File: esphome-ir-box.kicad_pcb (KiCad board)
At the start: 2 copper layers, 32 x 55.8 mm, 16 parts, among them J1 Conn_01x15_Female, J2 Conn_01x15_Female, J3 Conn_01x15_Male, J4 Conn_01x15_Male, Q1 2N7000, Q2 2N7000, Q3 2N7000, U1 VS1838B

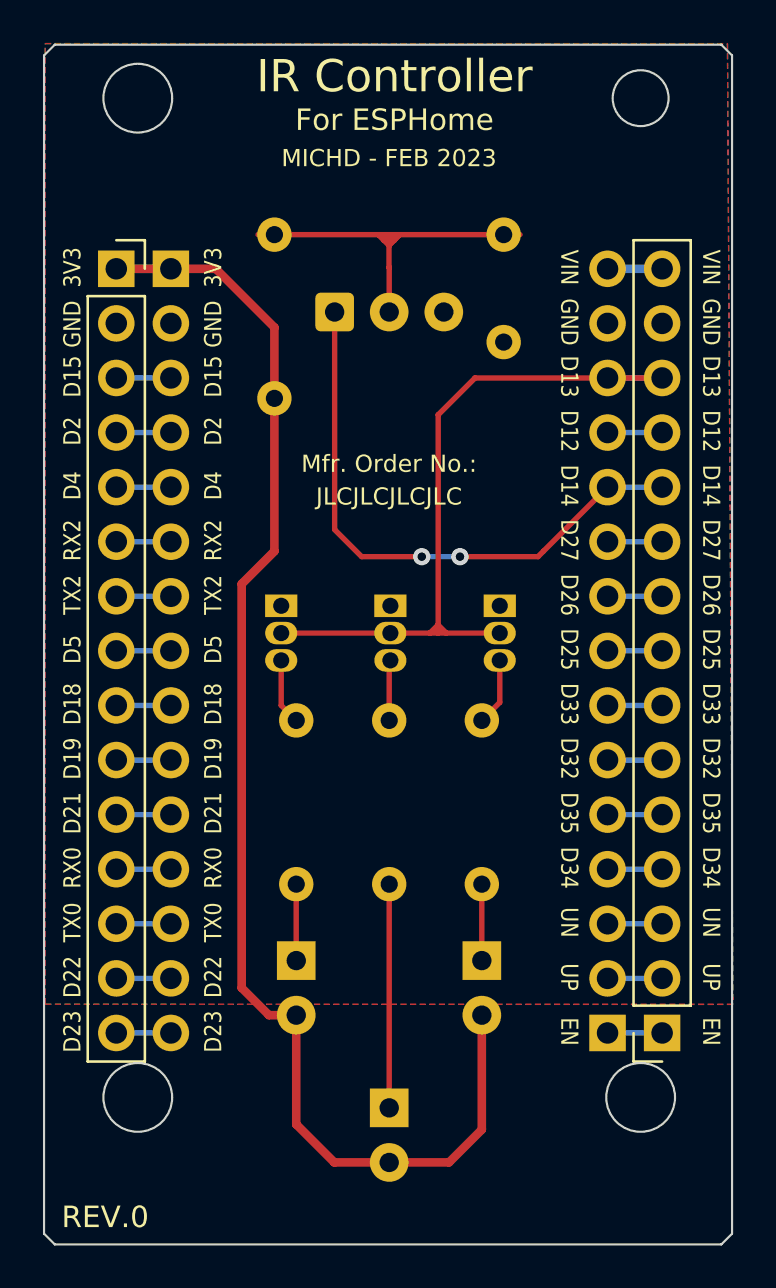
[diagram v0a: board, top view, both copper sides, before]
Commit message: Fix VS1813B pinout, KiCad 7 tweaks
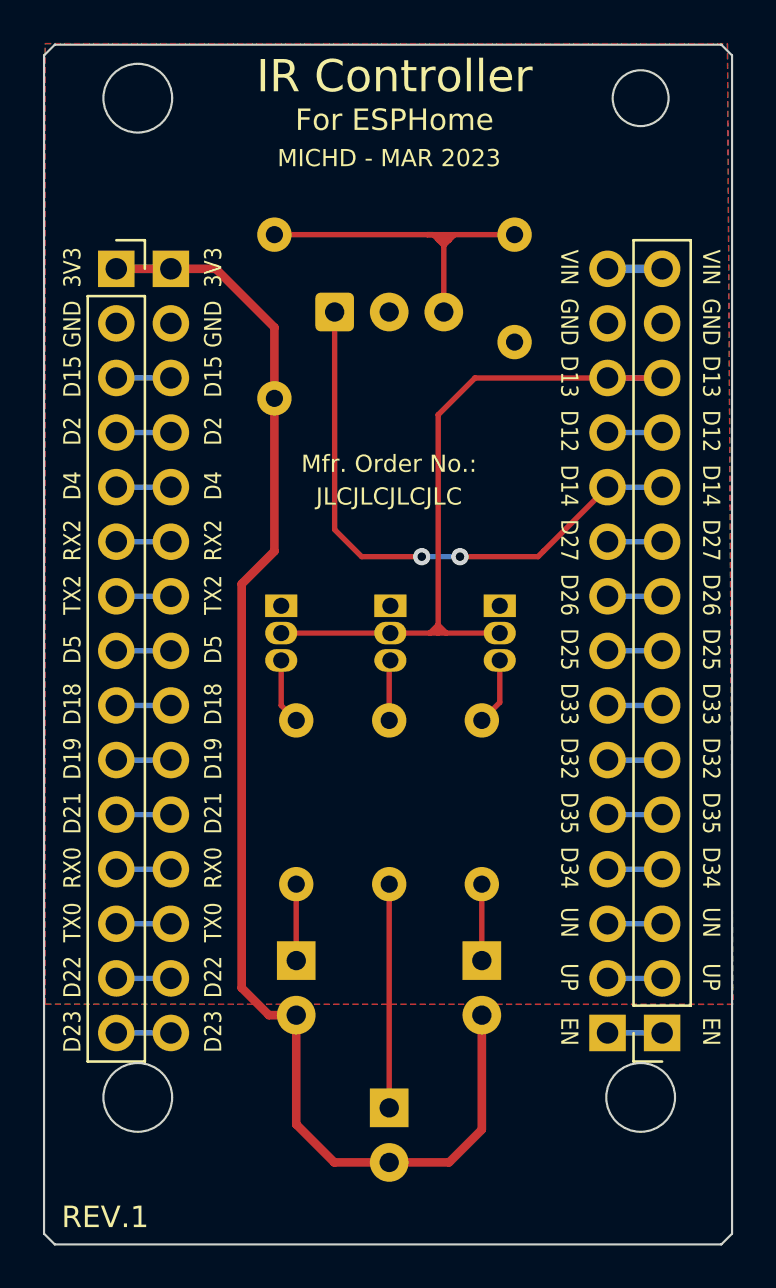
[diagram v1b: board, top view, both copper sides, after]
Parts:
- moved C1 0.51 mm to (152.1, 67.6)
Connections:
- C1 pad 1: Net-(C1-Pad1) -> Net-(U1-Vs)
- R4 pad 2: Net-(C1-Pad1) -> Net-(U1-Vs)
- U1 pad 2: Net-(C1-Pad1) -> GND
- U1 pad 3: GND -> Net-(U1-Vs)
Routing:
- net Net-(C1-Pad1): track 18.0 -> 0.00 mm
- net Net-(U1-Vs): track 0.00 -> 17.2 mm
- added copper zone on F.Cu, net GND
- removed copper zone on F.Cu, net +5V
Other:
- board text added: "MICHD - MAR 2023"
- board text added: "REV.1"
- board text removed: "MICHD - FEB 2023"
- board text removed: "REV.0"

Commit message: Revise board, focussing on building into devices
New board layout has very few onboard components, and focuses on wiring
an IR LED into an existing device (next to its sensor), while leeching
power of the host device and piggybacking off its IR sensor.

There are jumpers for selecting input voltage (5V or 3.3V) which
determines where power gets routed to on the esp32 dev board, as well as
a bypassable voltage divider for the IR input. So if the host device
runs the IR sensor at 5V, it is selectable on this board, so it's
lowered to ~3.3V before going into the ESP32.

The IR Led connection to resistor/esp32 is also optional with a pair of
jumpers, so the connector can be used for other purposes if needed.

Lastly, there's a "protoboard" area for a small bit of custom circuitry
/ connectors, along with several power connection points.
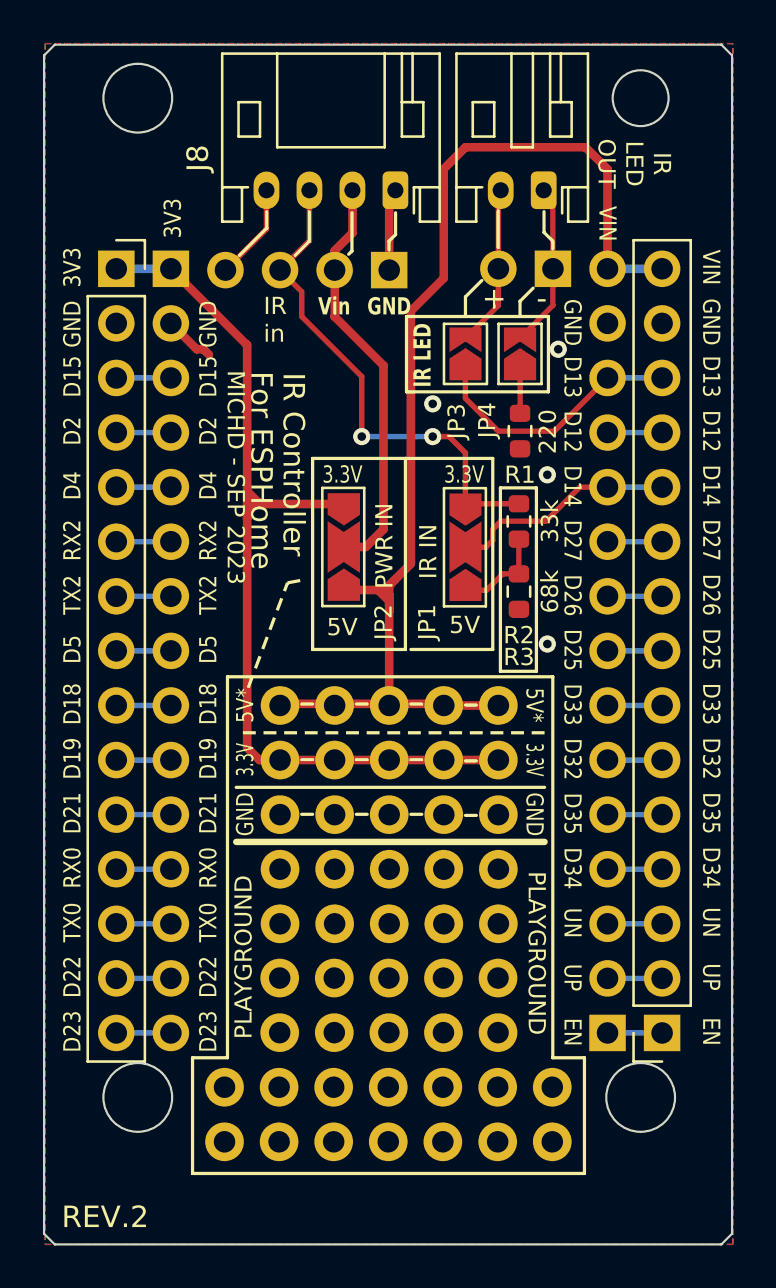
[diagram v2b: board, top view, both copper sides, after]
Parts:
- removed C1: 100n, Capacitor_THT:C_Disc_D4.7mm_W2.5mm_P5.00mm
- removed D1, D2, D3: LED, LED_THT:LED_D5.0mm_Clear
- removed Q1, Q2, Q3: 2N7000, Package_TO_SOT_THT:TO-92_Inline
- removed R4: 100, Resistor_THT:R_Axial_DIN0207_L6.3mm_D2.5mm_P7.62mm_Horizontal
- removed U1: VS1838B, OptoDevice:Vishay_MOLD-3Pin
- added ?: , , F.Cu at (151.4, 104.7)
- added ?: , , F.Cu at (146.5, 102.1)
- added ?: , , F.Cu at (146.5, 109.7)
- added ?: , , F.Cu at (151.4, 92.1)
- added ?: , , F.Cu at (151.4, 102.2)
- added ?: , , F.Cu at (144.1, 97.0)
- added ?: , , F.Cu at (149.9, 97.0)
- added ?: , , F.Cu at (149.9, 109.7)
- added ?: , , F.Cu at (146.5, 107.2)
- added ?: , , F.Cu at (138.8, 107.1)
- added ?: , , F.Cu at (151.3, 109.8)
- added ?: , , F.Cu at (146.6, 97.0)
- added ?: , , F.Cu at (151.4, 94.6)
- added ?: , , F.Cu at (144.1, 107.2)
- added ?: , , F.Cu at (153.8, 107.3)
- added ?: , , F.Cu at (149.9, 107.2)
- added ?: , , F.Cu at (149.9, 94.5)
- added ?: , , F.Cu at (138.6, 109.8)
- added ?: , , F.Cu at (144.1, 89.4)
- added ?: , , F.Cu at (149.9, 102.1)
- added ?: , , F.Cu at (149.9, 91.9)
- added ?: , , F.Cu at (153.9, 109.8)
- added ?: , , F.Cu at (146.5, 104.6)
- added ?: , , F.Cu at (144.1, 91.9)
- added ?: , , F.Cu at (151.4, 99.6)
- added ?: , , F.Cu at (151.3, 107.3)
- added ?: , , F.Cu at (144.1, 104.6)
- added ?: , , F.Cu at (146.6, 99.6)
- added ?: , , F.Cu at (146.6, 89.4)
- added ?: , , F.Cu at (149.9, 89.4)
- added ?: , , F.Cu at (149.9, 104.6)
- added ?: , , F.Cu at (151.4, 89.4)
- added ?: , , F.Cu at (144.1, 102.1)
- added ?: , , F.Cu at (144.1, 109.7)
- added ?: , , F.Cu at (146.6, 91.9)
- added ?: , , F.Cu at (149.9, 99.6)
- added ?: , , F.Cu at (144.1, 99.6)
- added ?: , , F.Cu at (151.4, 97.1)
- added ?: , , F.Cu at (144.1, 94.5)
- added ?: , , F.Cu at (146.6, 94.5)
- added J5: Conn_01x04_Pin, Connector_PinHeader_2.54mm:PinHeader_1x04_P2.54mm_Vertical, F.Cu at (146.3, 69.2)
- added J6: Conn_01x02_Pin, Connector_JST:JST_PH_S2B-PH-K_1x02_P2.00mm_Horizontal, F.Cu at (153.5, 65.5)
- added J7: Conn_01x02_Pin, Connector_PinHeader_2.54mm:PinHeader_1x02_P2.54mm_Vertical, F.Cu at (153.9, 69.2)
- added J8: Conn_01x04_Pin, Connector_JST:JST_PH_S4B-PH-K_1x04_P2.00mm_Horizontal, F.Cu at (146.6, 65.5)
- added JP1: Jumper_3_Bridged12, Jumper:SolderJumper-3_P2.0mm_Open_TrianglePad1.0x1.5mm, F.Cu at (149.9, 82.1)
- added JP2: Jumper_3_Bridged12, Jumper:SolderJumper-3_P2.0mm_Open_TrianglePad1.0x1.5mm, F.Cu at (144.2, 82.1)
- added JP3: Jumper_2_Open, Jumper:SolderJumper-2_P1.3mm_Open_TrianglePad1.0x1.5mm, F.Cu at (149.9, 73.1)
- added JP4: Jumper_2_Open, Jumper:SolderJumper-2_P1.3mm_Open_TrianglePad1.0x1.5mm, F.Cu at (152.4, 73.1)
- added REF**: Pin_D0.9mm_L10.0mm_W2.4mm_FlatFork, Connector_Pin:Pin_D0.9mm_L10.0mm_W2.4mm_FlatFork, F.Cu at (142.0, 108.4)
- added REF**: Pin_D0.9mm_L10.0mm_W2.4mm_FlatFork, Connector_Pin:Pin_D0.9mm_L10.0mm_W2.4mm_FlatFork, F.Cu at (142.0, 100.8)
- added REF**: Pin_D0.9mm_L10.0mm_W2.4mm_FlatFork, Connector_Pin:Pin_D0.9mm_L10.0mm_W2.4mm_FlatFork, F.Cu at (142.3, 90.2)
- added REF**: Pin_D0.9mm_L10.0mm_W2.4mm_FlatFork, Connector_Pin:Pin_D0.9mm_L10.0mm_W2.4mm_FlatFork, F.Cu at (142.0, 103.3)
- added REF**: Pin_D0.9mm_L10.0mm_W2.4mm_FlatFork, Connector_Pin:Pin_D0.9mm_L10.0mm_W2.4mm_FlatFork, F.Cu at (142.0, 93.2)
- added REF**: Pin_D0.9mm_L10.0mm_W2.4mm_FlatFork, Connector_Pin:Pin_D0.9mm_L10.0mm_W2.4mm_FlatFork, F.Cu at (142.0, 111.0)
- added REF**: Pin_D0.9mm_L10.0mm_W2.4mm_FlatFork, Connector_Pin:Pin_D0.9mm_L10.0mm_W2.4mm_FlatFork, F.Cu at (142.0, 95.8)
- added REF**: Pin_D0.9mm_L10.0mm_W2.4mm_FlatFork, Connector_Pin:Pin_D0.9mm_L10.0mm_W2.4mm_FlatFork, F.Cu at (142.0, 105.9)
- added REF**: Pin_D0.9mm_L10.0mm_W2.4mm_FlatFork, Connector_Pin:Pin_D0.9mm_L10.0mm_W2.4mm_FlatFork, F.Cu at (142.0, 98.3)
- R1: value 100 -> 220; footprint Resistor_THT:R_Axial_DIN0207_L6.3mm_D2.5mm_P7.62mm_Horizontal -> Resistor_SMD:R_0603_1608Metric; moved to F.Cu
- R2: value 100 -> 33k; footprint Resistor_THT:R_Axial_DIN0207_L6.3mm_D2.5mm_P7.62mm_Horizontal -> Resistor_SMD:R_0603_1608Metric; moved to F.Cu
- R3: value 100 -> 68k; footprint Resistor_THT:R_Axial_DIN0207_L6.3mm_D2.5mm_P7.62mm_Horizontal -> Resistor_SMD:R_0603_1608Metric; moved to F.Cu
- moved R1 21.2 mm to (152.4, 76.7), turned to -90 degrees
- moved R2 17.9 mm to (152.3, 80.9), turned to -90 degrees
- moved R3 17.1 mm to (152.3, 84.2), turned to -90 degrees
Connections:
- net /IR_SENSOR renamed /IR_SENSOR_UC
- R1 pad 2: Net-(Q1-D) -> GND
- R2 pad 1: Net-(D2-K) -> /IR_SENSOR_CONN
- R2 pad 2: Net-(Q2-D) -> Net-(JP1-A)
- R3 pad 1: Net-(D3-K) -> Net-(JP1-A)
- R3 pad 2: Net-(Q3-D) -> GND
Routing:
- net +5V: track 2.54 -> 56.4 mm
- net /IR_SENSOR_CONN: track 0.00 -> 23.6 mm, vias 0 -> 2
- net /IR_TX: track 35.1 -> 12.2 mm
- net +3.3V: track 65.9 -> 44.6 mm
- net VIN: track 0.00 -> 19.3 mm
- net Net-(U1-Vs): track 17.2 -> 0.00 mm
- net /IR_SENSOR_UC: track 27.2 -> 10.6 mm, vias 2 -> 0
- net Net-(D2-K): track 10.4 -> 0.00 mm
- net Net-(J6-Pin_1): track 0.00 -> 7.70 mm
- net Net-(J6-Pin_2): track 0.00 -> 7.57 mm
- net GND: track 0.00 -> 6.21 mm, vias 0 -> 4
- net Net-(J5-Pin_4): track 0.00 -> 4.51 mm
- net Net-(JP1-A): track 0.00 -> 4.42 mm
- net Net-(D3-K): track 3.56 -> 0.00 mm
- net Net-(Q1-D): track 3.14 -> 0.00 mm
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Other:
- board text added: "+"
- board text added: "-"
- board text added: "3.3V"
- board text added: "5V"
- board text added: "5V*"
- board text added: "Config jumpers on other side"
- board text added: "IR Controller For ESPHome MICHD - SEP 2023"
- board text added: "IR IN"
- board text added: "IR LED"
- board text added: "IR LED OUT"
- board text added: "IR in"
- board text added: "MICHD - SEP 2023"
- board text added: "PLAYGROUND"
- board text added: "PWR IN"
- board text added: "REV.2"
- board text added: "Vin"
- board text removed: "JLCJLCJLCJLC"
- board text removed: "MICHD - MAR 2023"
- board text removed: "Mfr. Order No.:"
- board text removed: "REV.1"

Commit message: Add JLC mfr order no placeholder
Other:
- board text added: "JLCJLCJLCJLC"
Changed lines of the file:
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@@
       (drillshape 0)
       (scaleselection 1)
-      (outputdirectory "outputs/rev1/")
+      (outputdirectory "outputs/rev2/")
     )
   )
@@
     (fp_line (start 3.95 6.25) (end 3.95 -1.35)
       (stroke (width 0.1) (type solid)) (layer "F.Fab"))
-    (pad "1" thru_hole roundrect (at 0 0 180) (size 1.2 1.75) (drill 0.75) (layers "*.Cu" "*.Mask") (roundrect_rratio 0.208333)
+    (pad "1" thru_hole roundrect (at 0 0 180) (size 1.2 1.75) (drill 0.75) (layers "*.Cu" "*.Mask") (roundrect_rratio 0.2083333333)
       (net 4 "Net-(J6-Pin_1)") (pinfunction "Pin_1") (pintype "passive"))
     (pad "2" thru_hole oval (at 2 0 180) (size 1.2 1.75) (drill 0.75) (layers "*.Cu" "*.Mask")
@@
     (fp_line (start 7.95 6.25) (end 7.95 -1.35)
       (stroke (width 0.1) (type solid)) (layer "F.Fab"))
-    (pad "1" thru_hole roundrect (at 0 0 180) (size 1.2 1.75) (drill 0.75) (layers "*.Cu" "*.Mask") (roundrect_rratio 0.208333)
+    (pad "1" thru_hole roundrect (at 0 0 180) (size 1.2 1.75) (drill 0.75) (layers "*.Cu" "*.Mask") (roundrect_rratio 0.2083333333)
       (net 2 "GND") (pinfunction "Pin_1") (pintype "passive"))
     (pad "2" thru_hole oval (at 2 0 180) (size 1.2 1.75) (drill 0.75) (layers "*.Cu" "*.Mask")
@@
     (effects (font (size 1 1) (thickness 0.15)) (justify left bottom mirror))
   )
+  (gr_text "JLCJLCJLCJLC" (at 130.81 114.046) (layer "B.SilkS")
+    (effects (font (size 0.8 0.8) (thickness 0.13)) (justify right bottom mirror))
+  )
   (gr_text "VIN" (at 156.5 67 270) (layer "B.SilkS")
